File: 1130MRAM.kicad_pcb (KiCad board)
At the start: 2 copper layers, 203.2 x 63.5 mm, 123 parts, among them J1 Screw_Terminal_01x02, J1A09 SLTpad, J1A11 SLTpad, K1E09 SLTpad, K1E11 SLTpad, M1A09 SLTpad, M1A11 SLTpad, M1C09 SLTpad, M1D09 SLTpad, M1E09 SLTpad, M1E11 SLTpad, SW1 SLTpad, U1 MR0A16AYS35, U10 74LS09, U11 74LS09, U12 SN74LVC1G123DCUR, U13 SN74LVC1G123DCUR, U14 74LS00, U2 SN74LVC244APWR, U3 SN74LVC244APWR, U4 LT8642S, U5 SN74LVC1G123DCUR, U6 SN74LVC1G123DCUR, U7 74LS09, U8 74LS09, U9 74LS09

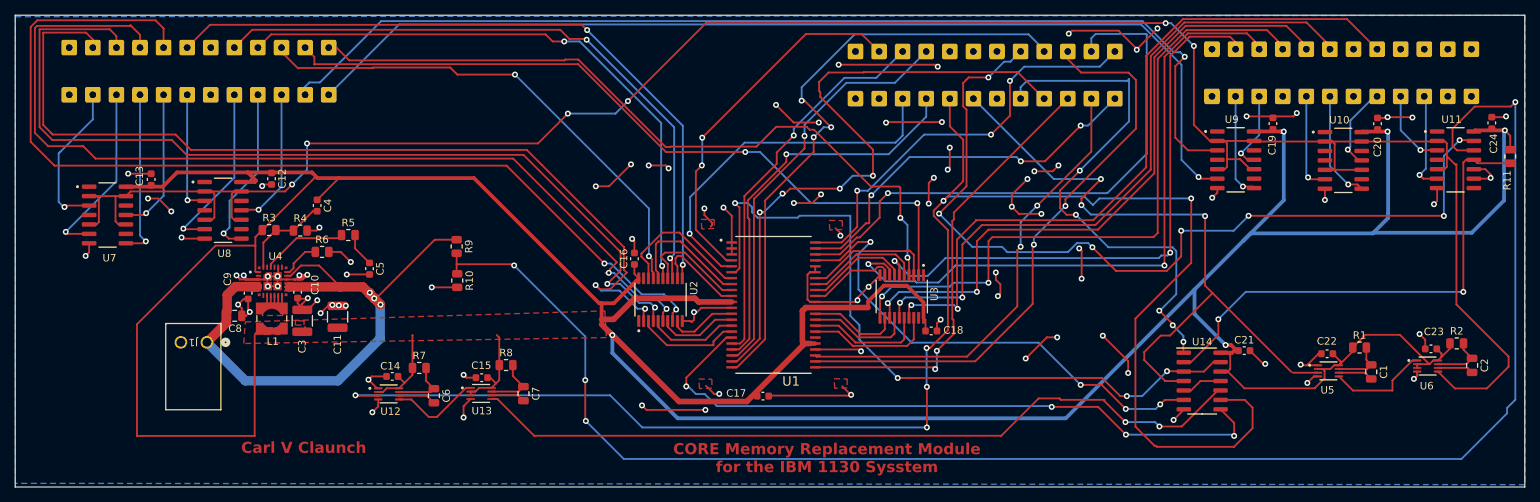
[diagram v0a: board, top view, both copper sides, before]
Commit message: Completed design V1
prior to verification
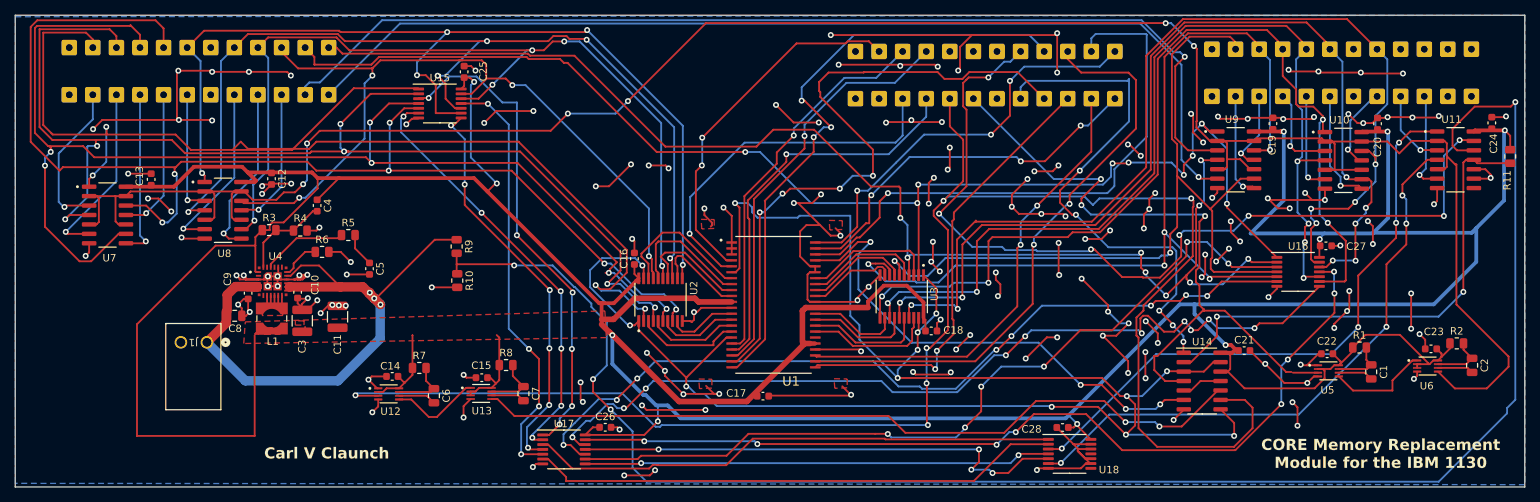
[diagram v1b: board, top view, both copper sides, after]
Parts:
- added C25: 0.1uF, Capacitor_SMD:C_0603_1608Metric, F.Cu at (106.2, 63.5)
- added C26: 0.1uF, Capacitor_SMD:C_0603_1608Metric, F.Cu at (125.2, 111.3)
- added C27: 0.1uF, Capacitor_SMD:C_0603_1608Metric, F.Cu at (222.2, 86.9)
- added C28: 0.1uF, Capacitor_SMD:C_0603_1608Metric, F.Cu at (186.7, 111.4)
- added U15: 74LS86, Package_SO:TSSOP-14_4.4x5mm_P0.65mm, F.Cu at (102.9, 67.8)
- added U16: 74LS86, Package_SO:TSSOP-14_4.4x5mm_P0.65mm, F.Cu at (218.4, 90.4)
- added U17: 74LS86, Package_SO:TSSOP-14_4.4x5mm_P0.65mm, F.Cu at (119.6, 114.3)
- added U18: 74LS86, Package_SO:TSSOP-14_4.4x5mm_P0.65mm, F.Cu at (187.7, 114.9)
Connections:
- S12 pad 1: unconnected-(S12-Pin_1-Pad1) -> Net-(S12-Pin_1)
- U1 pad 17: Net-(U1-~{W}) -> Net-(U1-~{E})
- U10 pad 1: unconnected-(U10-Pad1) -> Net-(B12-Pin_1)
- U10 pad 12: unconnected-(U10-Pad12) -> Net-(B15-Pin_1)
- U10 pad 3: unconnected-(U10-Pad3) -> Net-(S12-Pin_1)
- U10 pad 4: unconnected-(U10-Pad4) -> Net-(B13-Pin_1)
- U10 pad 9: unconnected-(U10-Pad9) -> Net-(B14-Pin_1)
- U11 pad 1: unconnected-(U11-Pad1) -> Net-(U11-Pad1)
- U11 pad 4: unconnected-(U11-Pad4) -> Net-(U11-Pad4)
- U14 pad 8: Net-(U1-~{W}) -> Net-(U1-~{E})
- U2 pad 1: unconnected-(U2-~{1OE}-Pad1) -> Net-(U1-~{E})
- U2 pad 19: unconnected-(U2-~{2OE}-Pad19) -> Net-(U1-~{E})
- U3 pad 1: unconnected-(U3-~{1OE}-Pad1) -> Net-(U1-~{E})
- U3 pad 19: unconnected-(U3-~{2OE}-Pad19) -> Net-(U1-~{E})
- U4 pad 29: (no net) -> unconnected-(U4-T1-Pad29)
- U4 pad 30: (no net) -> unconnected-(U4-T2-Pad30)
- U4 pad 31: (no net) -> unconnected-(U4-T3-Pad31)
- U4 pad 32: (no net) -> unconnected-(U4-T4-Pad32)
- U7 pad 1: unconnected-(U7-Pad1) -> Net-(B0-Pin_1)
- U7 pad 12: unconnected-(U7-Pad12) -> Net-(B3-Pin_1)
- U7 pad 4: unconnected-(U7-Pad4) -> Net-(B1-Pin_1)
- U7 pad 9: unconnected-(U7-Pad9) -> Net-(B2-Pin_1)
- U8 pad 1: unconnected-(U8-Pad1) -> Net-(B4-Pin_1)
- U8 pad 12: unconnected-(U8-Pad12) -> Net-(B7-Pin_1)
- U8 pad 4: unconnected-(U8-Pad4) -> Net-(B5-Pin_1)
- U8 pad 9: unconnected-(U8-Pad9) -> Net-(B6-Pin_1)
- U9 pad 1: unconnected-(U9-Pad1) -> Net-(B8-Pin_1)
- U9 pad 12: unconnected-(U9-Pad12) -> Net-(B11-Pin_1)
- U9 pad 4: unconnected-(U9-Pad4) -> Net-(B9-Pin_1)
- U9 pad 9: unconnected-(U9-Pad9) -> Net-(B10-Pin_1)
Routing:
- net GND: track 279.1 -> 554.4 mm, vias 90 -> 169
- net Net-(U1-~{E}): track 98.0 -> 244.9 mm, vias 4 -> 13
- net Net-(U16-Pad11): track 0.00 -> 123.2 mm, vias 0 -> 8
- net Net-(U16-Pad8): track 0.00 -> 118.8 mm, vias 0 -> 10
- net Net-(U16-Pad6): track 0.00 -> 112.8 mm, vias 0 -> 8
- net Net-(U16-Pad3): track 0.00 -> 110.3 mm, vias 0 -> 6
- net Net-(U1-~{W}): track 90.4 -> 0.00 mm, vias 4 -> 0
- net Net-(U11-Pad1): track 0.00 -> 81.4 mm, vias 0 -> 4
- net Net-(U11-Pad4): track 0.00 -> 79.7 mm, vias 0 -> 4
- net +3.3V: track 546.0 -> 625.5 mm, vias 5 -> 10
- net Net-(B9-Pin_1): track 100.2 -> 175.9 mm, vias 2 -> 9
- net Net-(B8-Pin_1): track 101.5 -> 176.0 mm, vias 2 -> 9
- net Net-(U17-Pad6): track 0.00 -> 71.6 mm
- net Net-(U17-Pad3): track 0.00 -> 71.1 mm
- net Net-(U17-Pad11): track 0.00 -> 67.5 mm, vias 0 -> 4
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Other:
- board text added: "CORE Memory Replacement Module for the IBM 1130"
- board text added: "T1"
- board text added: "T3"
- board text added: "T4"
- board text removed: "CORE Memory Replacement Module for the IBM 1130 Sysstem"

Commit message: Latest version with fixes
fixed parity circuits, went to 4 layer board
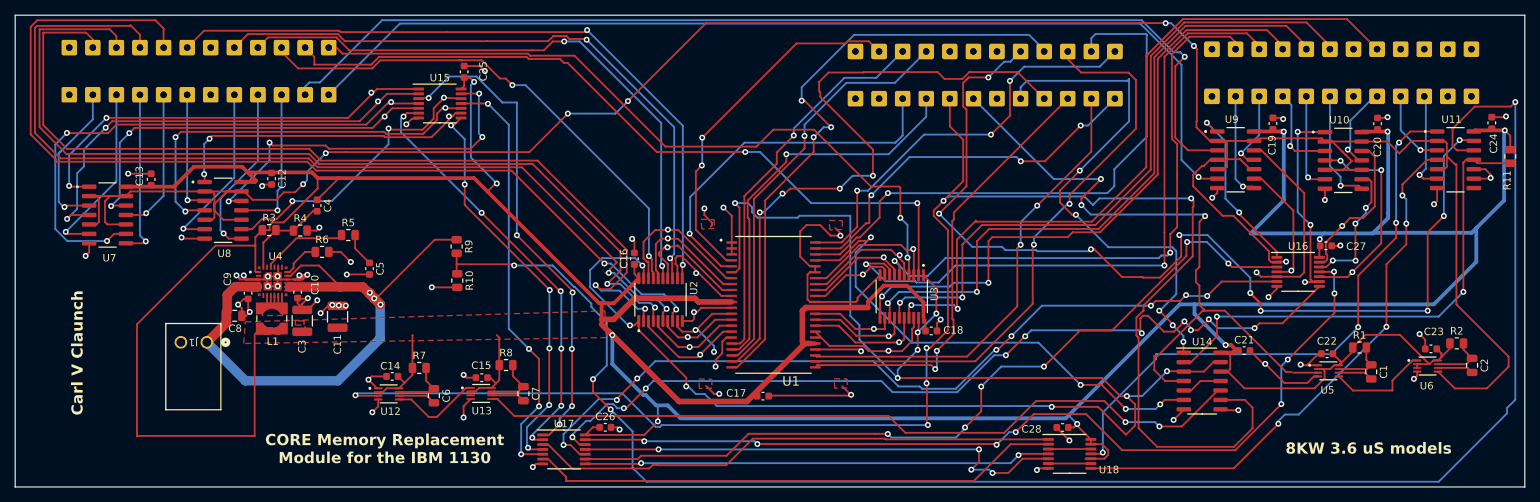
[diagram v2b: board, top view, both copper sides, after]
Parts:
- U2, U3: value SN74LVC244APWR -> SN74LV240APWR
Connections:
- U1 pad 17: Net-(U1-~{E}) -> Net-(U1-~{W})
- U10 pad 1: Net-(B12-Pin_1) -> Net-(U1-DQU12)
- U10 pad 12: Net-(B15-Pin_1) -> Net-(U1-DQU15)
- U10 pad 4: Net-(B13-Pin_1) -> Net-(U1-DQU13)
- U10 pad 9: Net-(B14-Pin_1) -> Net-(U1-DQU14)
- U14 pad 8: Net-(U1-~{E}) -> Net-(U1-~{W})
- U15 pad 1: Net-(B0-Pin_1) -> Net-(U1-DQL0)
- U15 pad 10: Net-(B5-Pin_1) -> Net-(U1-DQL5)
- U15 pad 12: Net-(B6-Pin_1) -> Net-(U1-DQL6)
- U15 pad 13: Net-(B7-Pin_1) -> Net-(U1-DQL7)
- U15 pad 2: Net-(B1-Pin_1) -> Net-(U1-DQL1)
- U15 pad 4: Net-(B2-Pin_1) -> Net-(U1-DQL2)
- U15 pad 5: Net-(B3-Pin_1) -> Net-(U1-DQL3)
- U15 pad 9: Net-(B4-Pin_1) -> Net-(U1-DQL4)
- U16 pad 1: Net-(B8-Pin_1) -> Net-(U1-DQU8)
- U16 pad 10: Net-(B13-Pin_1) -> Net-(U1-DQU13)
- U16 pad 12: Net-(B14-Pin_1) -> Net-(U1-DQU14)
- U16 pad 13: Net-(B15-Pin_1) -> Net-(U1-DQU15)
- U16 pad 2: Net-(B9-Pin_1) -> Net-(U1-DQU9)
- U16 pad 4: Net-(B10-Pin_1) -> Net-(U1-DQU10)
- U16 pad 5: Net-(B11-Pin_1) -> Net-(U1-DQU11)
- U16 pad 9: Net-(B12-Pin_1) -> Net-(U1-DQU12)
- U18 pad 10: GND -> +3.3V
- U18 pad 11: unconnected-(U18-Pad11) -> Net-(U11-Pad1)
- U18 pad 12: GND -> Net-(U18-Pad12)
- U18 pad 13: GND -> +3.3V
- U18 pad 3: Net-(U11-Pad1) -> Net-(U18-Pad12)
- U18 pad 6: Net-(U11-Pad4) -> Net-(U18-Pad6)
- U18 pad 8: unconnected-(U18-Pad8) -> Net-(U11-Pad4)
- U18 pad 9: GND -> Net-(U18-Pad6)
- U7 pad 1: Net-(B0-Pin_1) -> Net-(U1-DQL0)
- U7 pad 12: Net-(B3-Pin_1) -> Net-(U1-DQL3)
- U7 pad 4: Net-(B1-Pin_1) -> Net-(U1-DQL1)
- U7 pad 9: Net-(B2-Pin_1) -> Net-(U1-DQL2)
- U8 pad 1: Net-(B4-Pin_1) -> Net-(U1-DQL4)
- U8 pad 12: Net-(B7-Pin_1) -> Net-(U1-DQL7)
- U8 pad 4: Net-(B5-Pin_1) -> Net-(U1-DQL5)
- U8 pad 9: Net-(B6-Pin_1) -> Net-(U1-DQL6)
- U9 pad 1: Net-(B8-Pin_1) -> Net-(U1-DQU8)
- U9 pad 12: Net-(B11-Pin_1) -> Net-(U1-DQU11)
- U9 pad 4: Net-(B9-Pin_1) -> Net-(U1-DQU9)
- U9 pad 9: Net-(B10-Pin_1) -> Net-(U1-DQU10)
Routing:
- net GND: track 554.4 -> 197.2 mm, vias 169 -> 57
- net Net-(U1-DQL2): track 15.2 -> 138.4 mm, vias 0 -> 4
- net Net-(U1-DQU8): track 17.3 -> 140.2 mm, vias 0 -> 3
- net Net-(U1-DQL1): track 17.5 -> 131.1 mm, vias 0 -> 4
- net Net-(U1-DQL0): track 19.6 -> 130.1 mm, vias 0 -> 4
- net Net-(U1-DQL3): track 12.8 -> 123.3 mm, vias 0 -> 4
- net Net-(U1-DQL5): track 10.7 -> 116.5 mm, vias 0 -> 4
- net Net-(U1-DQL7): track 14.1 -> 113.5 mm, vias 0 -> 5
- net Net-(U1-DQL4): track 9.36 -> 106.5 mm, vias 0 -> 5
- net Net-(U1-DQU13): track 13.9 -> 109.3 mm, vias 0 -> 4
- net Net-(U1-DQU12): track 11.9 -> 104.4 mm, vias 0 -> 4
- net Net-(U1-DQL6): track 12.2 -> 101.4 mm, vias 0 -> 4
- net Net-(U1-DQU9): track 16.0 -> 102.2 mm, vias 0 -> 2
- net Net-(U1-DQU14): track 15.7 -> 99.0 mm, vias 0 -> 5
- net Net-(U1-DQU11): track 12.3 -> 95.4 mm, vias 0 -> 2
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- added copper zone on In2.Cu, net GND
- removed copper zone on B.Cu, net GND
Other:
- copper layers 2 -> 4
- board text added: "8KW 3.6 uS models"

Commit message: Annotations and cleanup
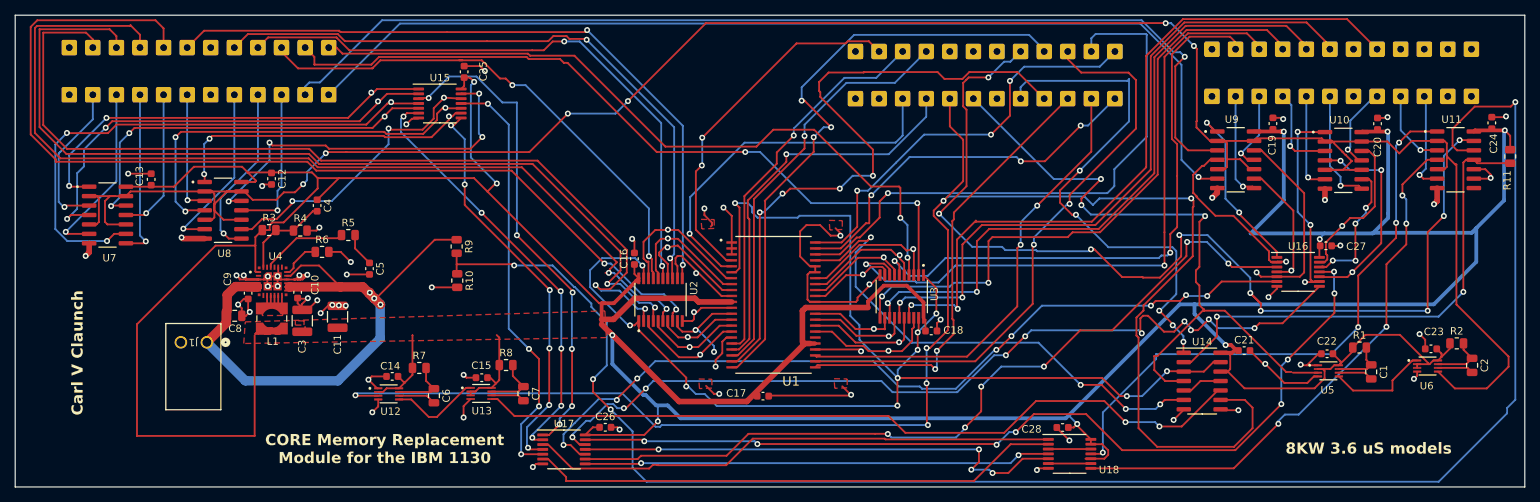
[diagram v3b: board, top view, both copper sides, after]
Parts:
- C1, C6: value 500pF -> 470pF
- C2, C7: value 50pF -> 47pF
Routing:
- net Net-(U1-~{E}): track 217.6 -> 182.9 mm
- net Net-(U1-DQU9): track 102.2 -> 102.8 mm
- net GND: track 197.2 -> 197.3 mm, vias 57 -> 58

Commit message: Corrections to design
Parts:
- removed R11: 10K, Resistor_SMD:R_0805_2012Metric
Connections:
- SS1 pad 1: Net-(SS1-Pin_1) -> unconnected-(SS1-Pin_1-Pad1)
- U11 pad 11: Net-(R11-Pad1) -> unconnected-(U11-Pad11)
- U11 pad 12: Net-(R10-Pad1) -> GND
- U11 pad 13: Net-(SS1-Pin_1) -> GND
- U14 pad 2: Net-(R11-Pad1) -> Net-(R10-Pad1)
- U2 pad 1: Net-(U1-~{E}) -> Net-(U1-~{W})
- U2 pad 19: Net-(U1-~{E}) -> Net-(U1-~{W})
- U3 pad 1: Net-(U1-~{E}) -> Net-(U1-~{W})
- U3 pad 19: Net-(U1-~{E}) -> Net-(U1-~{W})
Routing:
- net Net-(SS1-Pin_1): track 138.1 -> 0.00 mm, vias 9 -> 0
- net Net-(U1-~{E}): track 182.9 -> 98.1 mm, vias 11 -> 4
- net Net-(R10-Pad1): track 229.8 -> 161.3 mm, vias 4 -> 5
- net Net-(R11-Pad1): track 67.2 -> 0.00 mm, vias 2 -> 0
- net Net-(U1-~{W}): track 81.1 -> 135.2 mm, vias 2 -> 7
- net GND: track 197.3 -> 202.5 mm
- net +3.3V: track 632.7 -> 629.9 mm
- net unconnected-(SS1-Pin_1-Pad1): track 0.00 -> 0.82 mm

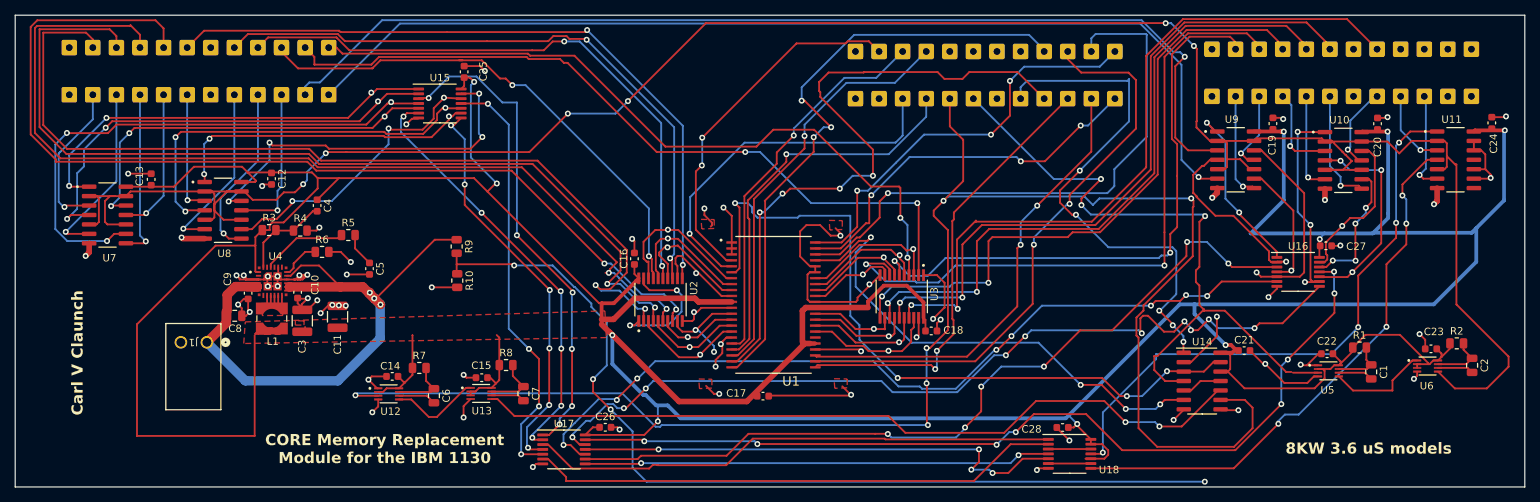
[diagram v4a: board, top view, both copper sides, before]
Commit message: Debugged version of KiCAD files
Created project library for the symbols and footprints used with this design
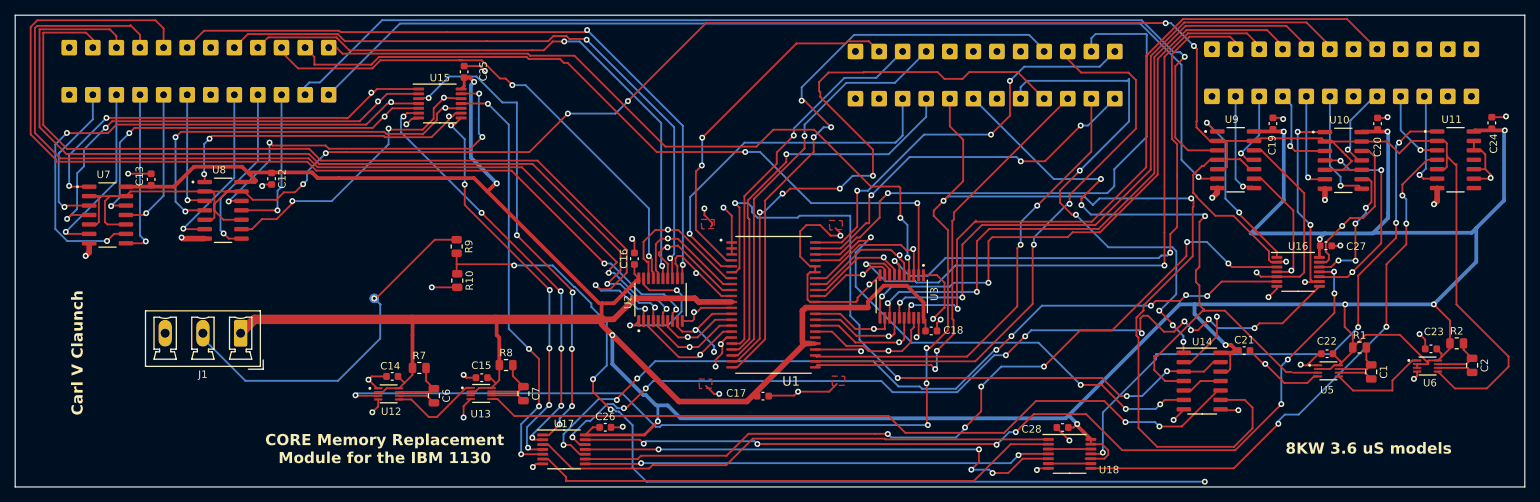
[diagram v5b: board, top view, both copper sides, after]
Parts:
- removed C10, C9: 200pF, Capacitor_SMD:C_0603_1608Metric
- removed C11, C3: 22uF, Capacitor_SMD:C_1210_3225Metric
- removed C4: 47pF, Capacitor_SMD:C_0603_1608Metric
- removed C5: 470pF, Capacitor_SMD:C_0603_1608Metric
- removed C8: 4.7uF, Capacitor_SMD:C_0805_2012Metric
- removed L1: 1.7uH, Inductor_SMD:L_Wuerth_WE-TPC-3816
- removed R3: 100K, Resistor_SMD:R_0805_2012Metric
- removed R4: 22.1K, Resistor_SMD:R_0805_2012Metric
- removed R5: 15K, Resistor_SMD:R_0805_2012Metric
- removed R6: 41.2K, Resistor_SMD:R_0805_2012Metric
- removed U4: LT8642S, Library.carl:LT8642SEV
- A1E09, A1E11, B0, B1, B10, B11, B12, B13, B14, B15, B2, B3, B4, B5, B6, B7, B8, B9, C1A09, C1A11, G1E09, G1E11, H1A11, H1D09, H1E09, J1A09, J1A11, K1E09, K1E11, M1A09, M1A11, M1C09, M1D09, M1E09, M1E11, N1A09, N1A11, S0, S1, S10, S11, S12, S13, S14, S15, S16, S17, S2, S3, S4, S5, S6, S7, S8, S9, SAR10, SAR11, SAR12, SAR13, SAR14, SAR15, SAR3, SAR4, SAR5, SAR6, SAR7, SAR8, SAR9, SR1, SS1, SU1, SW1: footprint Library.carl:SLT -> 1130MRAM:SLT
- C1, C6: value 470pF -> 680pF
- C2, C7: value 47pF -> 33pF
- J1: value Screw_Terminal_01x02 -> Screw_Terminal_01x03; footprint Library.carl:CONN2 screw -> Connector_Phoenix_MC_HighVoltage:PhoenixContact_MCV_1,5_3-G-5.08_1x03_P5.08mm_Vertical
- U10, U11, U7, U8, U9: value 74LS09 -> 74LS03; footprint Library.carl:sn74lc09dr -> 1130MRAM:sn74lc03dr
- U12, U13, U5, U6: footprint Library.carl:sn74lvc1g123dcur -> 1130MRAM:sn74lvc1g123dcur
- U2, U3: footprint Library.carl:sn74lvc244a -> 1130MRAM:sn74lvc244a
- moved J1 8.28 mm to (76.1, 98.7)
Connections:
- J1 pad 1: Net-(J1-Pin_1) -> +3.3V
- J1 pad 2: GND -> Net-(J1-Pin_2)
- R9 pad 1: Net-(J1-Pin_1) -> Net-(J1-Pin_2)
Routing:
- net Net-(J1-Pin_1): track 94.1 -> 0.00 mm, vias 3 -> 0
- net GND: track 202.5 -> 152.6 mm, vias 58 -> 39
- net Net-(J1-Pin_2): track 0.00 -> 48.0 mm, vias 0 -> 1
- net +3.3V: track 629.9 -> 587.1 mm, vias 10 -> 12
- net Net-(U4-FB): track 12.4 -> 0.00 mm
- net Net-(U4-VC): track 11.6 -> 0.00 mm
- net Net-(L1-Pad1): track 6.37 -> 0.00 mm
- net Net-(U4-RT): track 5.33 -> 0.00 mm
- net Net-(C5-Pad1): track 4.56 -> 0.00 mm
- net Net-(U1-DQU14): track 99.0 -> 99.8 mm
- removed copper zone on F.Cu, net +3.3V
- removed copper zone on F.Cu, net Net-(L1-Pad1)
